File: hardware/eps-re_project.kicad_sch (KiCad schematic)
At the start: 20 parts, among them J1 2053380004, J13 53398-0671, J14 53398-0471, J2 2053380004, J21 205338-0002, J22 205338-0002, J25 205338-0002, J26 205338-0002, J27 205338-0002, J28 205338-0002, J29 205338-0002, J3 53398-0471, J4 2053380004, J5 53398-0471, J6 53398-0471, J7 53398-0471

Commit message: hardware: Test points added
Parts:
- added TP2: AMUX[15..0], symbol Connector:TestPoint
- added TP2: BC_B_~{EN}, symbol Connector:TestPoint
- added TP2: BC_A_~{EN}, symbol Connector:TestPoint
- added TP2: AMUX[11..8], symbol Connector:TestPoint
- added TP2: 3V3_B_~{EN}, symbol Connector:TestPoint
- added TP2: 5V0_A_~{EN}, symbol Connector:TestPoint
- added TP2: 3V3_OBDH, symbol Connector:TestPoint
- added TP2: VBUS, symbol Connector:TestPoint
- added TP2 (x2): BC_VFB, symbol Connector:TestPoint
- added TP2: AMUX_OUT, symbol Connector:TestPoint
- added TP2: Payload_EN, symbol Connector:TestPoint
- added TP2: 5V0_Payload, symbol Connector:TestPoint
- added TP2: 5V0_RadioBeacon, symbol Connector:TestPoint
- added TP2: OBDH_EN, symbol Connector:TestPoint
- added TP2: AMUX[5..4], symbol Connector:TestPoint
- added TP2: RadioMain_EN, symbol Connector:TestPoint
- added TP2: 3V3, symbol Connector:TestPoint
- added TP2: BC_B_TS, symbol Connector:TestPoint
- added TP2: BC_A_TS, symbol Connector:TestPoint
- added TP2: AMUX[3..0], symbol Connector:TestPoint
- added TP2: VPANELS, symbol Connector:TestPoint
- added TP2: 3V3_AntDep, symbol Connector:TestPoint
- added TP2: VIN, symbol Connector:TestPoint
- added TP2: AMUX_SEL[3..0]AMUX[15..0], symbol Connector:TestPoint
- added TP2: 5V0_RadioMain, symbol Connector:TestPoint
- added TP2: Beacon_EN, symbol Connector:TestPoint
- added TP2: AntDep_EN, symbol Connector:TestPoint
- added TP2: 3V3_A_~{EN}, symbol Connector:TestPoint
- added TP2: 5V0_B_~{EN}, symbol Connector:TestPoint
- added TP2: AMUX[15..12], symbol Connector:TestPoint
- added TP2: VBAT, symbol Connector:TestPoint
- added TP2: 5V0, symbol Connector:TestPoint
- added TP2: RadioBeacon_EN, symbol Connector:TestPoint
- added TP2: 3V3_Beacon, symbol Connector:TestPoint
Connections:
- net 3V3_A_~{EN}: now also TP2.1
- net 3V3_AntDep: now also TP2.1
- net 3V3_B_~{EN}: now also TP2.1
- net 3V3_Beacon: now also TP2.1
- net 3V3_OBDH: now also TP2.1
- net 5V0_A_~{EN}: now also TP2.1
- net 5V0_B_~{EN}: now also TP2.1
- net 5V0_Payload: now also TP2.1
- net 5V0_RadioBeacon: now also TP2.1
- net 5V0_RadioMain: now also TP2.1
- net AMUX[11..8]: now also TP2.1
- net AMUX[15..0]: now also TP2.1
- net AMUX[15..12]: now also TP2.1
- net AMUX[3..0]: now also TP2.1
- net AMUX[5..4]: now also TP2.1
- net AMUX_OUT: now also TP2.1
- net AMUX_SEL[3..0]: now also TP2.1
- net AntDep_EN: now also TP2.1
- net BC_A_TS: now also TP2.1
- net BC_A_~{EN}: now also TP2.1
- net BC_B_TS: now also TP2.1
- net BC_B_~{EN}: now also TP2.1
- net BC_VFB: now also TP2.1, TP2.1
- net Beacon_EN: now also TP2.1
- net OBDH_EN: now also TP2.1
- net Payload_EN: now also TP2.1
- net RadioBeacon_EN: now also TP2.1
- net RadioMain_EN: now also TP2.1
- net VBUS: now also TP2.1
- net VIN: now also TP2.1
- new net 3V3: TP2.1
- new net 5V0: TP2.1
- new net VBAT: TP2.1
- new net VPANELS: TP2.1
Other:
- note added: "ALIMENTAÇÃO"
- note added: "ENABLES"
- note added: "MULTIPLEXADORES"

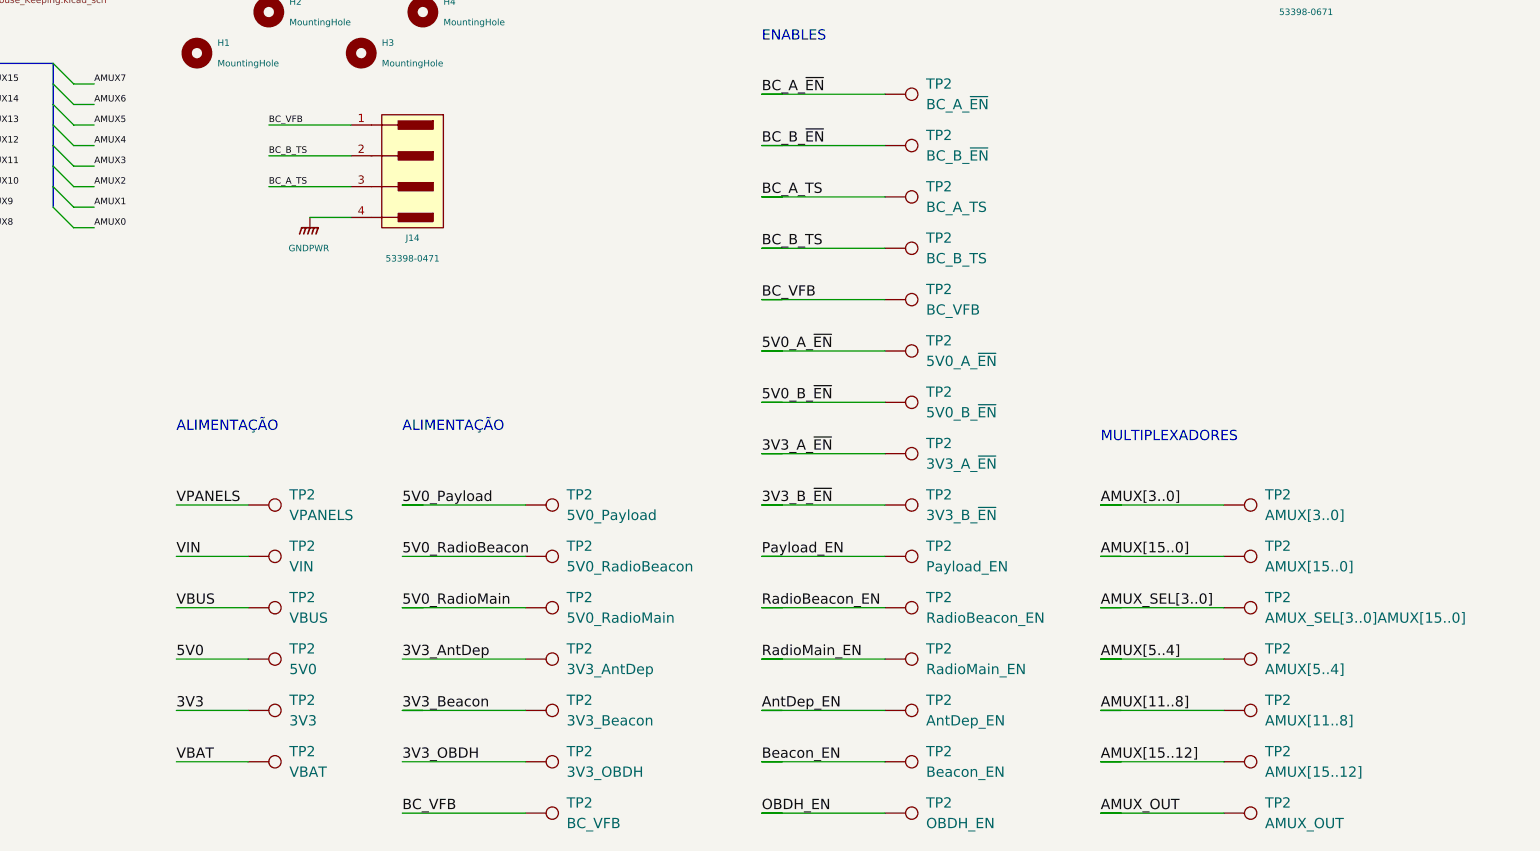
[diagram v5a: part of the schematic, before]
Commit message: hardware: Updating the custom design rules and library.
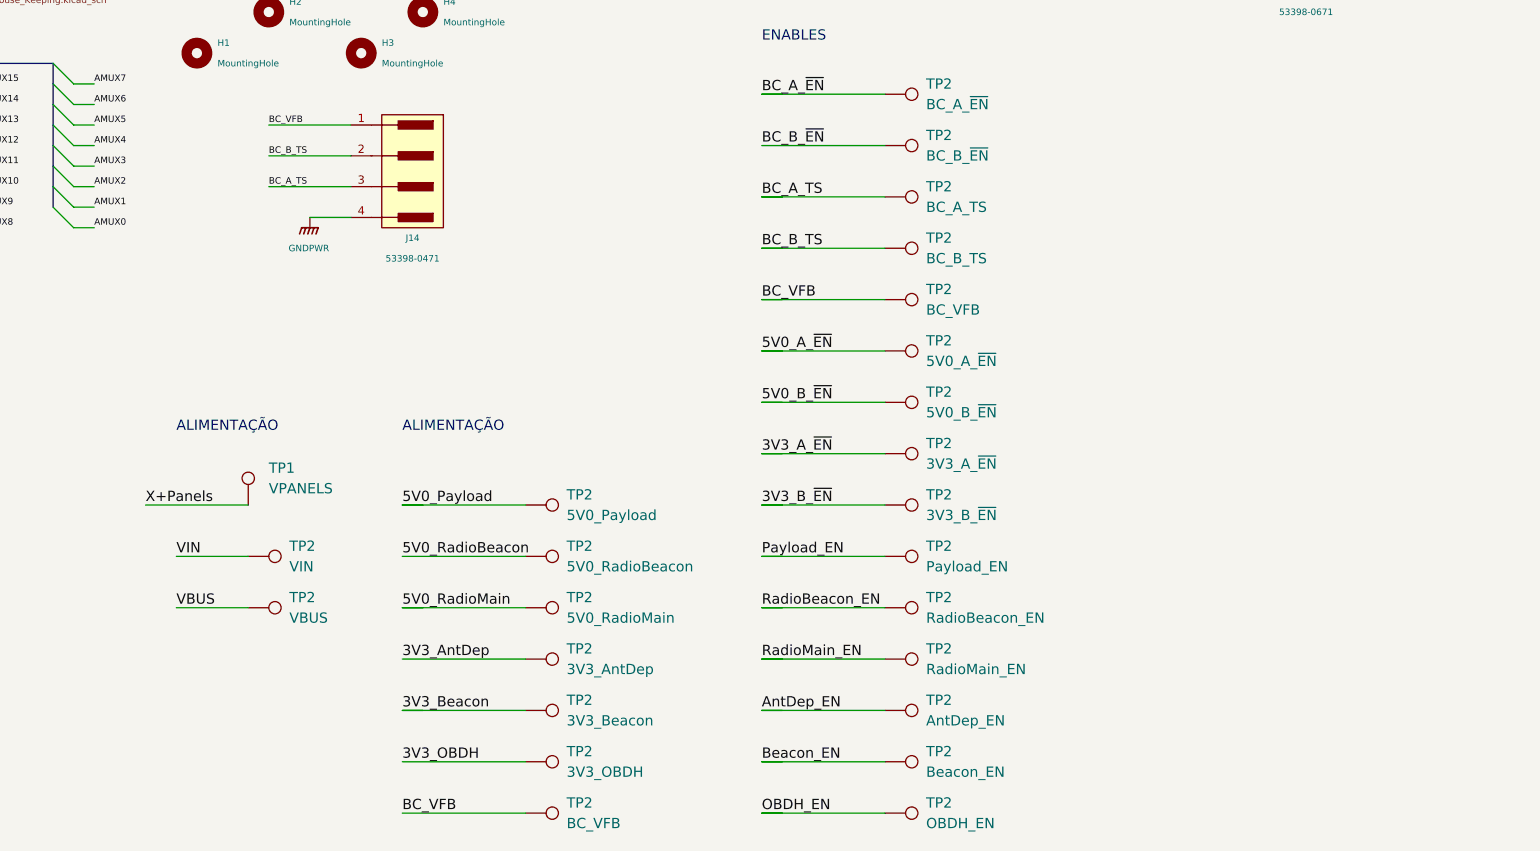
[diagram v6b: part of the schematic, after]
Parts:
- removed TP2: AMUX[15..0], symbol Connector:TestPoint
- removed TP2: AMUX[11..8], symbol Connector:TestPoint
- removed TP2: AMUX_OUT, symbol Connector:TestPoint
- removed TP2: AMUX[5..4], symbol Connector:TestPoint
- removed TP2: 3V3, symbol Connector:TestPoint
- removed TP2: AMUX[3..0], symbol Connector:TestPoint
- removed TP2: VPANELS, symbol Connector:TestPoint
- removed TP2: AMUX_SEL[3..0]AMUX[15..0], symbol Connector:TestPoint
- removed TP2: AMUX[15..12], symbol Connector:TestPoint
- removed TP2: VBAT, symbol Connector:TestPoint
- removed TP2: 5V0, symbol Connector:TestPoint
- added TP1: VPANELS, TestPoint:TestPoint_Pad_D1.0mm, symbol TESTPOINT:TestPoint
- TP2: footprint (none) -> TestPoint:TestPoint_Pad_D1.0mm; symbol Connector:TestPoint -> TESTPOINT:TestPoint
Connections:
- net X+Panels: now also TP1.1
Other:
- note removed: "MULTIPLEXADORES"

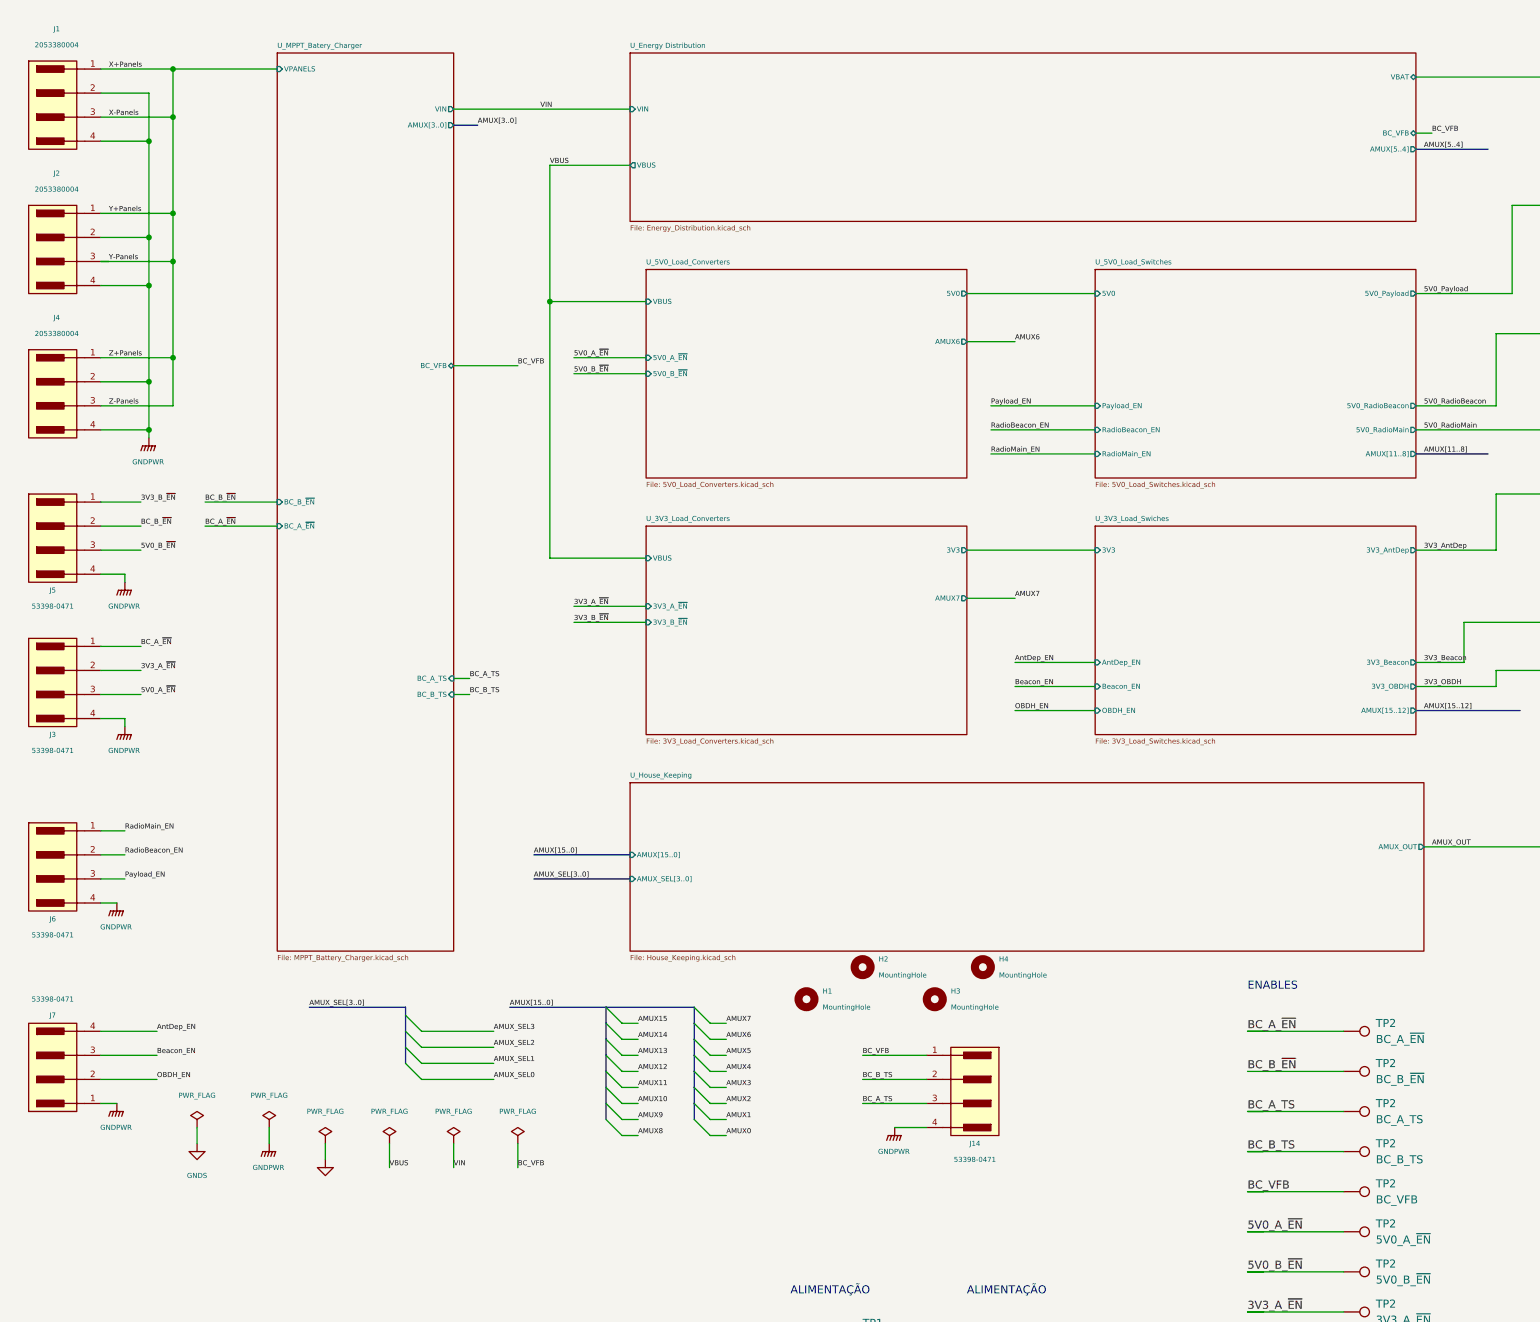
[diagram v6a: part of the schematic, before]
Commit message: hardware: Adding blocking diodes. Pass through diodes were also added in MPPT-based converters. Also, test points were added.
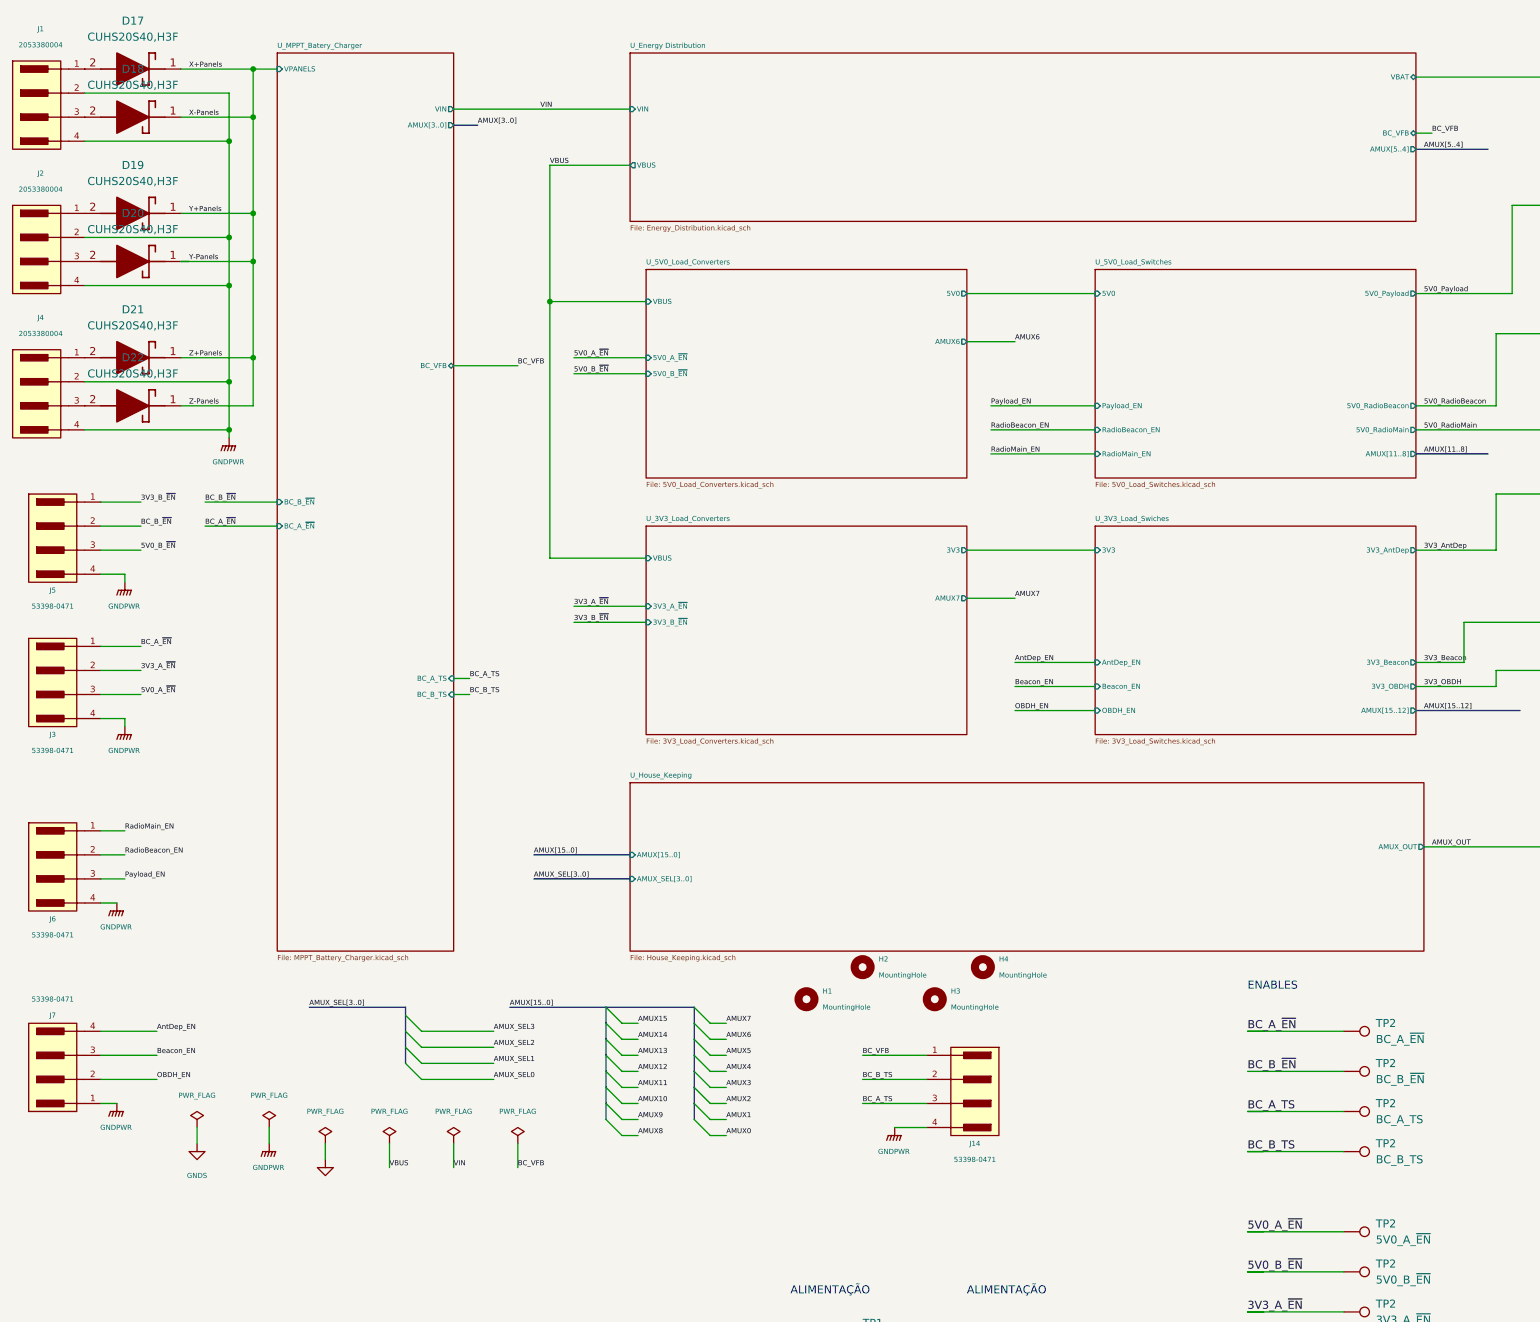
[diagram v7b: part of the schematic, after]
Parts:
- removed TP2: BC_VFB, TestPoint:TestPoint_Pad_D1.0mm, symbol TESTPOINT:TestPoint
- added D17, D18, D19, D20, D21, D22: CUHS20S40,H3F, footprints:CUHS20S40,H3F, symbol CUHS20S40,H3F:CUHS20S40,H3F
- TP1, TP2: footprint TestPoint:TestPoint_Pad_D1.0mm -> footprints:testpoint_smd
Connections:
- net X+Panels: now also D17.1 (K), D18.1 (K), D19.1 (K), D20.1 (K), D21.1 (K), D22.1 (K); no longer J1.1, J1.3, J2.1, J2.3, J4.1, J4.3
- new net: D17.2 (A), J1.1
- new net: D19.2 (A), J2.1
- new net: D18.2 (A), J1.3
- new net: D21.2 (A), J4.1
- new net: D20.2 (A), J2.3
- new net: D22.2 (A), J4.3
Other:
- moved on the sheet: J1, J2, J4

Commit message: hardware: Improving the readability of schematics
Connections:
- net X+Panels: now also D17.2 (A), J1.1; no longer D17.1 (K), D18.1 (K), D19.1 (K), D20.1 (K), D21.1 (K), D22.1 (K), TP1.1
- net Y+Panels: now reaches D19.2 (A), J2.1
- net X-Panels: now reaches D18.2 (A), J1.3
- net Z+Panels: now reaches D21.2 (A), J4.1
- net Y-Panels: now reaches D20.2 (A), J2.3
- net Z-Panels: now reaches D22.2 (A), J4.3
- new net VPANELS: D17.1 (K), D18.1 (K), D19.1 (K), D20.1 (K), D21.1 (K), D22.1 (K), TP1.1
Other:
- note added: "ANALOG SIGNALS"
- note added: "BLOCK DIAGRAM"
- note added: "MOUNTING HOLES"
- note added: "POWER FLAGS"
- note added: "REVISION HISTORY"
- note added: "TEST POINTS"
- note removed: "ALIMENTAÇÃO"
- note removed: "ENABLES"
- moved on the sheet: H1, H2, H3, H4, J13, J14, J21, J22, J25, J26, J27, J28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
